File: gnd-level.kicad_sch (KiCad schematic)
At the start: 6 parts, among them U5 ADS1015IDGS

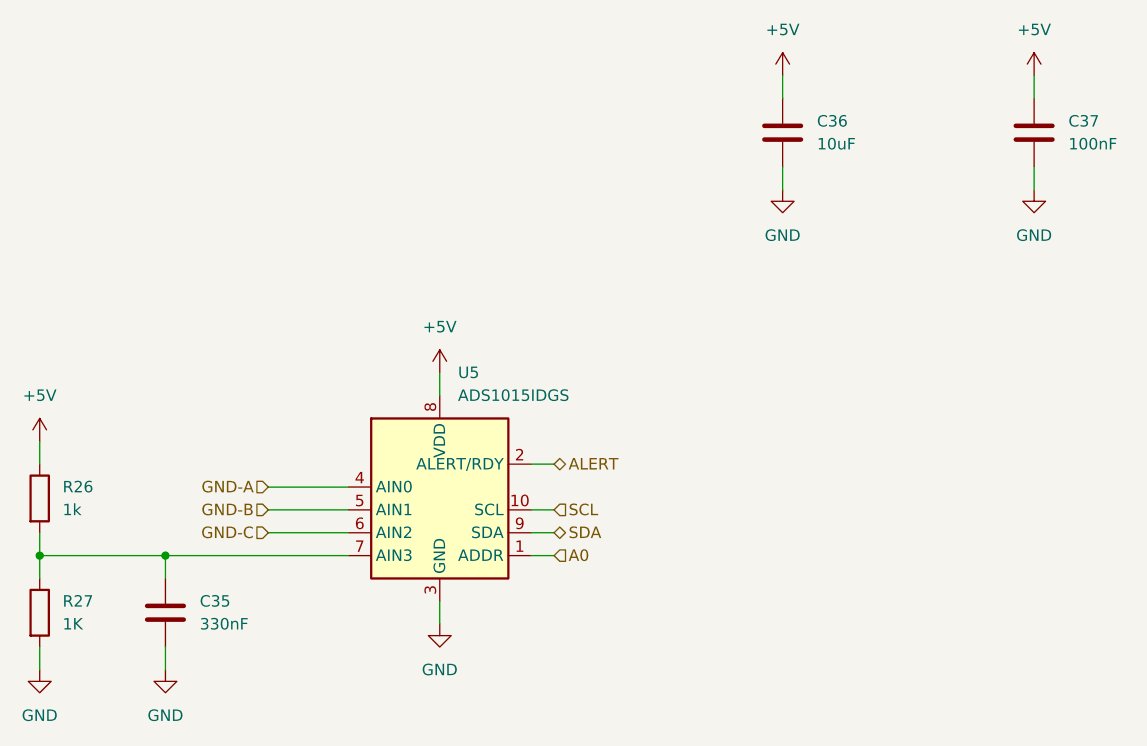
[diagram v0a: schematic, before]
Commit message: Add a lot of nice to haves
* Jumpers to bridge isolation
* I2C pullups with jumpers for input
* Labels on input connectors
* Geographic reference counts
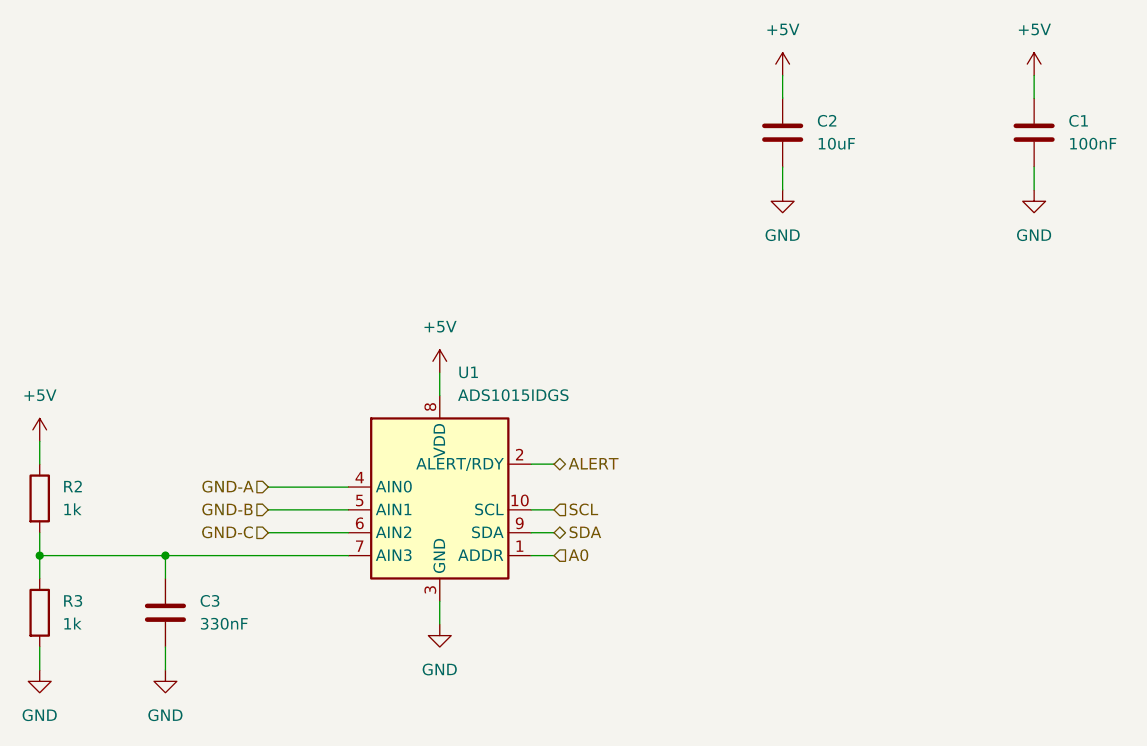
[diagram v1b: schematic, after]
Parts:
- R3: renamed from R27; value 1K -> 1k
- renumbered C37 to C1, C36 to C2, C35 to C3, R26 to R2, U5 to U1
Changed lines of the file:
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@@
   (symbol (lib_id "Device:C") (at 257.81 30.48 0) (unit 1)
     (in_bom yes) (on_board yes) (fields_autoplaced)
-    (property "Reference" "C37" (id 0) (at 261.62 29.2099 0)
+    (property "Reference" "C1" (id 0) (at 261.62 29.2099 0)
       (effects (font (size 1.27 1.27)) (justify left))
     )
@@
   (symbol (lib_id "Analog_ADC:ADS1015IDGS") (at 191.77 72.39 0) (unit 1)
     (in_bom yes) (on_board yes) (fields_autoplaced)
-    (property "Reference" "U5" (id 0) (at 193.7894 57.15 0)
+    (property "Reference" "U1" (id 0) (at 193.7894 57.15 0)
       (effects (font (size 1.27 1.27)) (justify left))
     )
@@
   (symbol (lib_id "Device:C") (at 161.29 83.82 0) (unit 1)
     (in_bom yes) (on_board yes) (fields_autoplaced)
-    (property "Reference" "C35" (id 0) (at 165.1 82.5499 0)
+    (property "Reference" "C3" (id 0) (at 165.1 82.5499 0)
       (effects (font (size 1.27 1.27)) (justify left))
     )
@@
   (symbol (lib_id "Device:R") (at 147.32 71.12 0) (unit 1)
     (in_bom yes) (on_board yes) (fields_autoplaced)
-    (property "Reference" "R26" (id 0) (at 149.86 69.8499 0)
+    (property "Reference" "R2" (id 0) (at 149.86 69.8499 0)
       (effects (font (size 1.27 1.27)) (justify left))
     )
@@
   (symbol (lib_id "Device:R") (at 147.32 83.82 0) (unit 1)
     (in_bom yes) (on_board yes) (fields_autoplaced)
-    (property "Reference" "R27" (id 0) (at 149.86 82.5499 0)
+    (property "Reference" "R3" (id 0) (at 149.86 82.5499 0)
       (effects (font (size 1.27 1.27)) (justify left))
     )
-    (property "Value" "1K" (id 1) (at 149.86 85.0899 0)
+    (property "Value" "1k" (id 1) (at 149.86 85.0899 0)
       (effects (font (size 1.27 1.27)) (justify left))
     )
@@
   (symbol (lib_id "Device:C") (at 229.87 30.48 0) (unit 1)
     (in_bom yes) (on_board yes) (fields_autoplaced)
-    (property "Reference" "C36" (id 0) (at 233.68 29.2099 0)
+    (property "Reference" "C2" (id 0) (at 233.68 29.2099 0)
       (effects (font (size 1.27 1.27)) (justify left))
     )

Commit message: Add LCSC order numbers to more easily order at JLCPCB
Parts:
- C1: LCSC Part # (none) -> C14663
- C2: LCSC Part # (none) -> C13585
- C3: LCSC Part # (none) -> C274377
- R2, R3: LCSC Part # (none) -> C4410
- U1: LCSC Part # (none) -> C193969
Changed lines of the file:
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@@
+      (effects (font (size 1.27 1.27)) hide)
+    )
+    (property "LCSC Part #" "C14663" (id 4) (at 257.81 30.48 0)
       (effects (font (size 1.27 1.27)) hide)
     )
@@
       (effects (font (size 1.27 1.27)) hide)
     )
+    (property "LCSC Part #" "C193969" (id 4) (at 191.77 72.39 0)
+      (effects (font (size 1.27 1.27)) hide)
+    )
     (pin "1")
     (pin "10")
@@
     )
     (property "Datasheet" "~" (id 3) (at 161.29 83.82 0)
+      (effects (font (size 1.27 1.27)) hide)
+    )
+    (property "LCSC Part #" "C274377" (id 4) (at 161.29 83.82 0)
       (effects (font (size 1.27 1.27)) hide)
     )
@@
       (effects (font (size 1.27 1.27)) hide)
     )
+    (property "LCSC Part #" "C4410" (id 4) (at 147.32 71.12 0)
+      (effects (font (size 1.27 1.27)) hide)
+    )
     (pin "1")
     (pin "2")
@@
       (effects (font (size 1.27 1.27)) hide)
     )
+    (property "LCSC Part #" "C4410" (id 4) (at 147.32 83.82 0)
+      (effects (font (size 1.27 1.27)) hide)
+    )
     (pin "1")
     (pin "2")
@@
       (effects (font (size 1.27 1.27)) hide)
     )
+    (property "LCSC Part #" "C13585" (id 4) (at 229.87 30.48 0)
+      (effects (font (size 1.27 1.27)) hide)
+    )

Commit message: Add JLCPCB rotation offsets
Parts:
- U1: JLCPCB Rotation Offset (none) -> -90
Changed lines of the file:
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@@
+      (effects (font (size 1.27 1.27)) hide)
+    )
+    (property "JLCPCB Rotation Offset" "-90" (id 5) (at 191.77 72.39 0)
       (effects (font (size 1.27 1.27)) hide)
     )

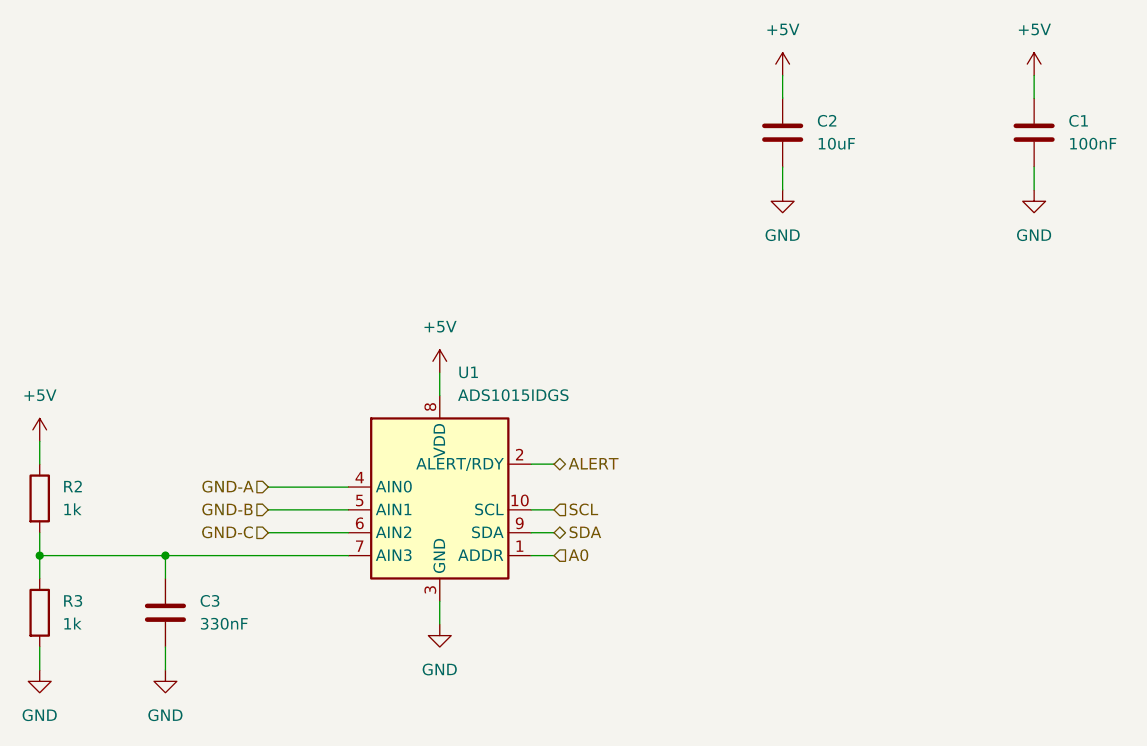
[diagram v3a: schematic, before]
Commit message: Shrink board and reduce features to reduce price
* Shrink to 100mm x 50mm
* Remove voltage regulator and use Stemma Power instead
* Remove isolation (is easier to add outside when needed)
* Remove reverse indicators to save space
* Remove I2C pullups as they are no longer needed
* Fix A2 of EEPROM and Temperature sensor to 0 to save space
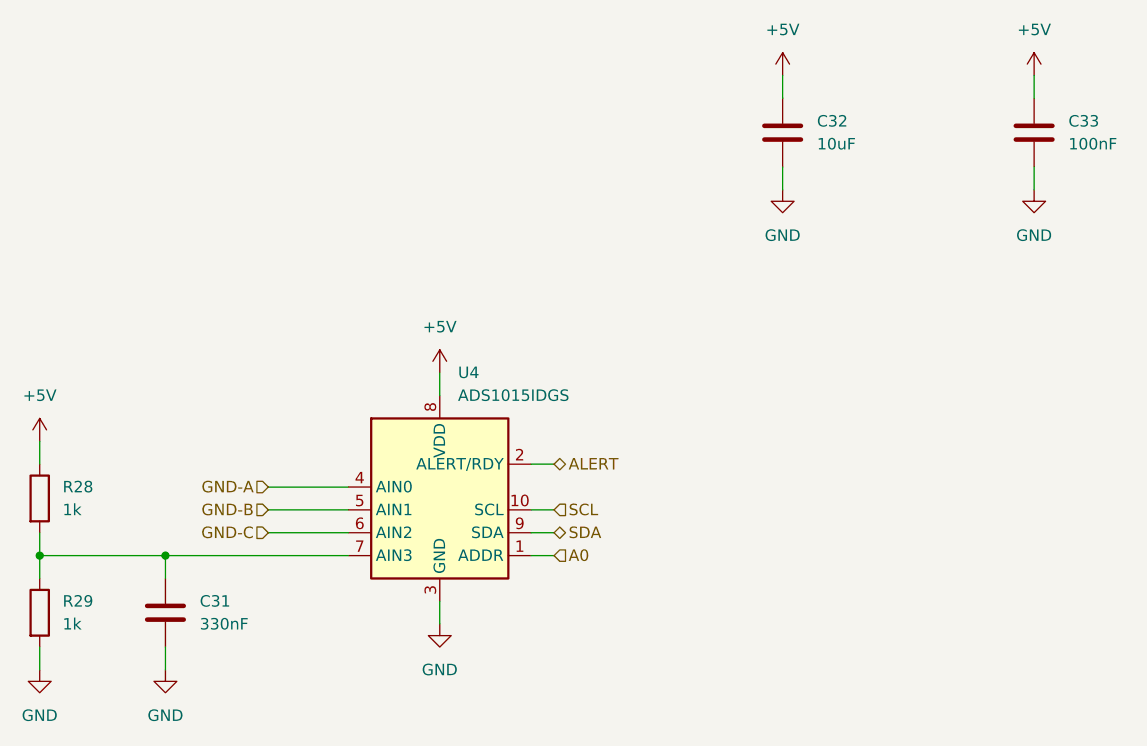
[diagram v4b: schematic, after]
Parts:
- renumbered C3 to C31, C2 to C32, C1 to C33, R2 to R28, R3 to R29, U1 to U4
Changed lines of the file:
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@@
   (symbol (lib_id "power:GND") (at 191.77 85.09 0) (unit 1)
     (in_bom yes) (on_board yes) (fields_autoplaced)
-    (property "Reference" "#PWR092" (id 0) (at 191.77 91.44 0)
+    (property "Reference" "#PWR082" (id 0) (at 191.77 91.44 0)
       (effects (font (size 1.27 1.27)) hide)
     )
@@
   (symbol (lib_id "Device:C") (at 257.81 30.48 0) (unit 1)
     (in_bom yes) (on_board yes) (fields_autoplaced)
-    (property "Reference" "C1" (id 0) (at 261.62 29.2099 0)
+    (property "Reference" "C33" (id 0) (at 261.62 29.2099 0)
       (effects (font (size 1.27 1.27)) (justify left))
     )
@@
   (symbol (lib_id "power:+5V") (at 191.77 57.15 0) (unit 1)
     (in_bom yes) (on_board yes) (fields_autoplaced)
-    (property "Reference" "#PWR091" (id 0) (at 191.77 60.96 0)
+    (property "Reference" "#PWR081" (id 0) (at 191.77 60.96 0)
       (effects (font (size 1.27 1.27)) hide)
     )
@@
   (symbol (lib_id "Analog_ADC:ADS1015IDGS") (at 191.77 72.39 0) (unit 1)
     (in_bom yes) (on_board yes) (fields_autoplaced)
-    (property "Reference" "U1" (id 0) (at 193.7894 57.15 0)
+    (property "Reference" "U4" (id 0) (at 193.7894 57.15 0)
       (effects (font (size 1.27 1.27)) (justify left))
     )
@@
   (symbol (lib_id "Device:C") (at 161.29 83.82 0) (unit 1)
     (in_bom yes) (on_board yes) (fields_autoplaced)
-    (property "Reference" "C3" (id 0) (at 165.1 82.5499 0)
+    (property "Reference" "C31" (id 0) (at 165.1 82.5499 0)
       (effects (font (size 1.27 1.27)) (justify left))
     )
@@
   (symbol (lib_id "power:+5V") (at 147.32 64.77 0) (unit 1)
     (in_bom yes) (on_board yes) (fields_autoplaced)
-    (property "Reference" "#PWR088" (id 0) (at 147.32 68.58 0)
+    (property "Reference" "#PWR078" (id 0) (at 147.32 68.58 0)
       (effects (font (size 1.27 1.27)) hide)
     )
@@
   (symbol (lib_id "power:GND") (at 147.32 90.17 0) (unit 1)
     (in_bom yes) (on_board yes) (fields_autoplaced)
-    (property "Reference" "#PWR089" (id 0) (at 147.32 96.52 0)
+    (property "Reference" "#PWR079" (id 0) (at 147.32 96.52 0)
       (effects (font (size 1.27 1.27)) hide)
     )
@@
   (symbol (lib_id "power:GND") (at 161.29 90.17 0) (unit 1)
     (in_bom yes) (on_board yes) (fields_autoplaced)
-    (property "Reference" "#PWR090" (id 0) (at 161.29 96.52 0)
+    (property "Reference" "#PWR080" (id 0) (at 161.29 96.52 0)
       (effects (font (size 1.27 1.27)) hide)
     )
@@
   (symbol (lib_id "Device:R") (at 147.32 71.12 0) (unit 1)
     (in_bom yes) (on_board yes) (fields_autoplaced)
-    (property "Reference" "R2" (id 0) (at 149.86 69.8499 0)
+    (property "Reference" "R28" (id 0) (at 149.86 69.8499 0)
       (effects (font (size 1.27 1.27)) (justify left))
     )
@@
   (symbol (lib_id "power:+5V") (at 229.87 24.13 0) (unit 1)
     (in_bom yes) (on_board yes) (fields_autoplaced)
-    (property "Reference" "#PWR093" (id 0) (at 229.87 27.94 0)
+    (property "Reference" "#PWR083" (id 0) (at 229.87 27.94 0)
       (effects (font (size 1.27 1.27)) hide)
     )
@@
   (symbol (lib_id "Device:R") (at 147.32 83.82 0) (unit 1)
     (in_bom yes) (on_board yes) (fields_autoplaced)
-    (property "Reference" "R3" (id 0) (at 149.86 82.5499 0)
+    (property "Reference" "R29" (id 0) (at 149.86 82.5499 0)
       (effects (font (size 1.27 1.27)) (justify left))
     )
@@
   (symbol (lib_id "Device:C") (at 229.87 30.48 0) (unit 1)
     (in_bom yes) (on_board yes) (fields_autoplaced)
-    (property "Reference" "C2" (id 0) (at 233.68 29.2099 0)
+    (property "Reference" "C32" (id 0) (at 233.68 29.2099 0)
       (effects (font (size 1.27 1.27)) (justify left))
     )
@@
   (symbol (lib_id "power:GND") (at 257.81 36.83 0) (unit 1)
     (in_bom yes) (on_board yes) (fields_autoplaced)
-    (property "Reference" "#PWR096" (id 0) (at 257.81 43.18 0)
+    (property "Reference" "#PWR086" (id 0) (at 257.81 43.18 0)
       (effects (font (size 1.27 1.27)) hide)
     )
@@
   (symbol (lib_id "power:+5V") (at 257.81 24.13 0) (unit 1)
     (in_bom yes) (on_board yes) (fields_autoplaced)
-    (property "Reference" "#PWR095" (id 0) (at 257.81 27.94 0)
+    (property "Reference" "#PWR085" (id 0) (at 257.81 27.94 0)
       (effects (font (size 1.27 1.27)) hide)
     )
@@
   (symbol (lib_id "power:GND") (at 229.87 36.83 0) (unit 1)
     (in_bom yes) (on_board yes) (fields_autoplaced)
-    (property "Reference" "#PWR094" (id 0) (at 229.87 43.18 0)
-      (effects (font (size 1.27 1.27)) hide)
-    )
+    (property "Reference" "#PWR084" (id 0) (at 229.87 43.18 0)
+      (effects (font (size 1.27 1.27)) hide)
+    )
